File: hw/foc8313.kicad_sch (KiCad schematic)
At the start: 56 parts, among them J1 Tag Connect, J2 CAN, J3 CAN, P1 USB_C_Plug, SW1 SW_SPST, U1 DRV8313PWP, U10 XC6206P332MR, U2 STM32F103CBTx, U4 AS5047D, U6 TJA1044GT/3Z, U7 LMR36015SFBRNXR, X1 X322516MLB4SI

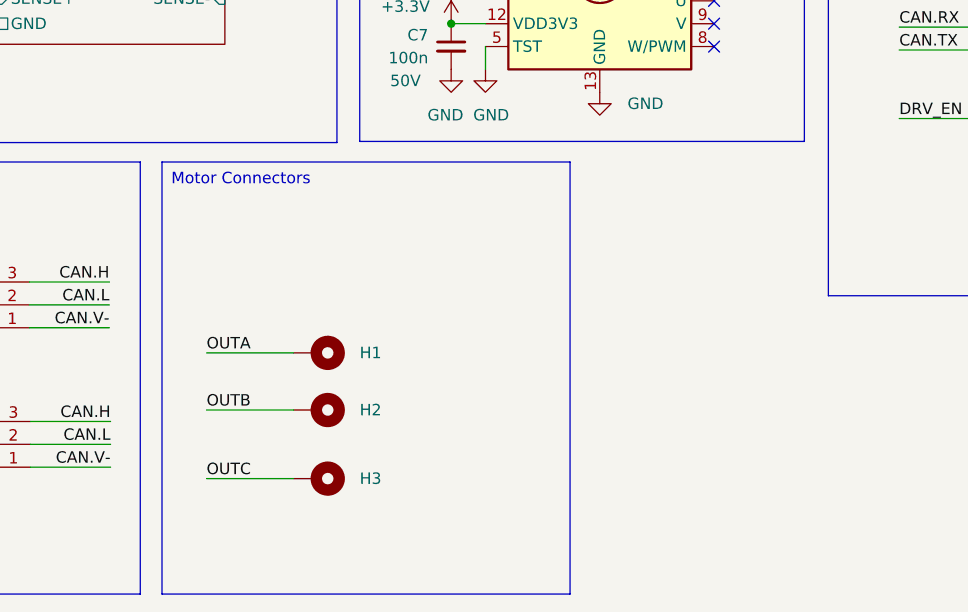
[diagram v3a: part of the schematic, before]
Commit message: [Hw] Rough incomplete layout and component placement
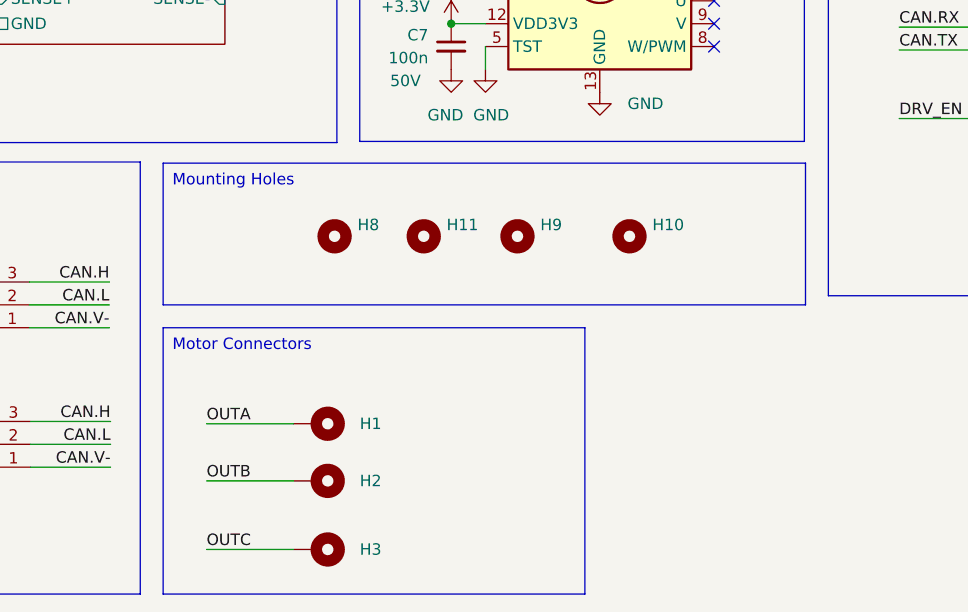
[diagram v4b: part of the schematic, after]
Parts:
- added H10, H11, H8, H9: MountingHole, MountingHole:MountingHole_3.2mm_M3_DIN965_Pad_TopOnly, symbol Mechanical:MountingHole
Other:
- moved on the sheet: H1, H2, H3
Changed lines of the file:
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@@
     (stroke (width 0) (type default))
   )
-  (wire (pts (xy 133.858 182.88) (xy 143.51 182.88))
+  (wire (pts (xy 133.858 190.754) (xy 143.51 190.754))
     (stroke (width 0) (type default))
   )
@@
     (stroke (width 0) (type default))
   )
-  (wire (pts (xy 133.858 175.26) (xy 143.51 175.26))
+  (wire (pts (xy 133.858 183.134) (xy 143.51 183.134))
     (stroke (width 0) (type default))
   )
@@
     (stroke (width 0) (type default))
   )
-  (wire (pts (xy 133.858 168.91) (xy 143.51 168.91))
+  (wire (pts (xy 133.858 176.784) (xy 143.51 176.784))
     (stroke (width 0) (type default))
   )
@@
   )
   (text_box "Motor Connectors\n"
-    (at 128.905 147.701 0) (size 45.339 48.006)
+    (at 129.032 166.116 0) (size 46.863 29.591)
+    (stroke (width 0) (type default))
+    (fill (type none))
+    (effects (font (size 1.27 1.27)) (justify left top))
+  )
+  (text_box "Mounting Holes\n"
+    (at 129.032 147.828 0) (size 71.374 15.748)
     (stroke (width 0) (type default))
     (fill (type none))
@@
     (effects (font (size 1.27 1.27)) (justify right bottom))
   )
-  (label "OUTC" (at 133.858 182.88 0) (fields_autoplaced)
+  (label "OUTC" (at 133.858 190.754 0) (fields_autoplaced)
     (effects (font (size 1.27 1.27)) (justify left bottom))
   )
@@
     (effects (font (size 1.27 1.27)) (justify right bottom))
   )
-  (label "OUTB" (at 133.858 175.26 0) (fields_autoplaced)
+  (label "OUTB" (at 133.858 183.134 0) (fields_autoplaced)
     (effects (font (size 1.27 1.27)) (justify left bottom))
   )
@@
     (effects (font (size 1.27 1.27)) (justify left bottom))
   )
-  (label "OUTA" (at 133.858 168.91 0) (fields_autoplaced)
+  (label "OUTA" (at 133.858 176.784 0) (fields_autoplaced)
     (effects (font (size 1.27 1.27)) (justify left bottom))
   )
@@
     )
   )
-  (symbol (lib_id "Mechanical:MountingHole_Pad") (at 146.05 182.88 270) (unit 1)
+  (symbol (lib_id "Mechanical:MountingHole_Pad") (at 146.05 190.754 270) (unit 1)
     (in_bom yes) (on_board yes) (dnp no) (fields_autoplaced)
-    (property "Reference" "H3" (at 150.876 182.88 90)
+    (property "Reference" "H3" (at 150.876 190.754 90)
       (effects (font (size 1.27 1.27)) (justify left))
     )
-    (property "Value" "MountingHole_Pad" (at 150.876 184.15 90)
+    (property "Value" "MountingHole_Pad" (at 150.876 192.024 90)
       (effects (font (size 1.27 1.27)) (justify left) hide)
     )
-    (property "Footprint" "local_lib:2x3" (at 146.05 182.88 0)
+    (property "Footprint" "local_lib:2x3" (at 146.05 190.754 0)
       (effects (font (size 1.27 1.27)) hide)
     )
-    (property "Datasheet" "~" (at 146.05 182.88 0)
+    (property "Datasheet" "~" (at 146.05 190.754 0)
       (effects (font (size 1.27 1.27)) hide)
     )
@@
     )
   )
+  (symbol (lib_id "Mechanical:MountingHole") (at 157.988 155.956 0) (unit 1)
+    (in_bom yes) (on_board yes) (dnp no) (fields_autoplaced)
+    (property "Reference" "H11" (at 160.528 154.686 0)
+      (effects (font (size 1.27 1.27)) (justify left))
+    )
+    (property "Value" "MountingHole" (at 160.528 157.226 0)
+      (effects (font (size 1.27 1.27)) (justify left) hide)
+    )
+    (property "Footprint" "MountingHole:MountingHole_3.2mm_M3_DIN965_Pad_TopOnly" (at 157.988 155.956 0)
+      (effects (font (size 1.27 1.27)) hide)
+    )
+    (property "Datasheet" "~" (at 157.988 155.956 0)
+      (effects (font (size 1.27 1.27)) hide)
+    )
+    (instances
+      (project "foc8313"
+        (path "/6a0f293a-1ae1-497a-a3c1-0d8f9e6f81b9"
+          (reference "H11") (unit 1)
+        )
+      )
+    )
+  )
   (symbol (lib_id "PCM_Diode_TVS_AKL:SMBJ48CA") (at 24.765 39.37 90) (unit 1)
     (in_bom yes) (on_board yes) (dnp no) (fields_autoplaced)
@@
     )
   )
+  (symbol (lib_id "Mechanical:MountingHole") (at 168.402 155.956 0) (unit 1)
+    (in_bom yes) (on_board yes) (dnp no) (fields_autoplaced)
+    (property "Reference" "H9" (at 170.942 154.686 0)
+      (effects (font (size 1.27 1.27)) (justify left))
+    )
+    (property "Value" "MountingHole" (at 170.942 157.226 0)
+      (effects (font (size 1.27 1.27)) (justify left) hide)
+    )
+    (property "Footprint" "MountingHole:MountingHole_3.2mm_M3_DIN965_Pad_TopOnly" (at 168.402 155.956 0)
+      (effects (font (size 1.27 1.27)) hide)
+    )
+    (property "Datasheet" "~" (at 168.402 155.956 0)
+      (effects (font (size 1.27 1.27)) hide)
+    )
+    (instances
+      (project "foc8313"
+        (path "/6a0f293a-1ae1-497a-a3c1-0d8f9e6f81b9"
+          (reference "H9") (unit 1)
+        )
+      )
+    )
+  )
   (symbol (lib_id "power:GND") (at 268.732 144.018 0) (unit 1)
     (in_bom yes) (on_board yes) (dnp no)
@@
     )
   )
+  (symbol (lib_id "Mechanical:MountingHole") (at 180.848 155.956 0) (unit 1)
+    (in_bom yes) (on_board yes) (dnp no) (fields_autoplaced)
+    (property "Reference" "H10" (at 183.388 154.686 0)
+      (effects (font (size 1.27 1.27)) (justify left))
+    )
+    (property "Value" "MountingHole" (at 183.388 157.226 0)
+      (effects (font (size 1.27 1.27)) (justify left) hide)
+    )
+    (property "Footprint" "MountingHole:MountingHole_3.2mm_M3_DIN965_Pad_TopOnly" (at 180.848 155.956 0)
+      (effects (font (size 1.27 1.27)) hide)
+    )
+    (property "Datasheet" "~" (at 180.848 155.956 0)
+      (effects (font (size 1.27 1.27)) hide)
+    )
+    (instances
+      (project "foc8313"
+        (path "/6a0f293a-1ae1-497a-a3c1-0d8f9e6f81b9"
+          (reference "H10") (unit 1)
+        )
+      )
+    )
+  )
   (symbol (lib_name "+3.3V_3") (lib_id "power:+3.3V") (at 105.41 84.074 0) (unit 1)
     (in_bom yes) (on_board yes) (dnp no)
@@
     )
   )
+  (symbol (lib_id "Mechanical:MountingHole") (at 148.082 155.956 0) (unit 1)
+    (in_bom yes) (on_board yes) (dnp no) (fields_autoplaced)
+    (property "Reference" "H8" (at 150.622 154.686 0)
+      (effects (font (size 1.27 1.27)) (justify left))
+    )
+    (property "Value" "MountingHole" (at 150.622 157.226 0)
+      (effects (font (size 1.27 1.27)) (justify left) hide)
+    )
+    (property "Footprint" "MountingHole:MountingHole_3.2mm_M3_DIN965_Pad_TopOnly" (at 148.082 155.956 0)
+      (effects (font (size 1.27 1.27)) hide)
+    )
+    (property "Datasheet" "~" (at 148.082 155.956 0)
+      (effects (font (size 1.27 1.27)) hide)
+    )
+    (instances
+      (project "foc8313"
+        (path "/6a0f293a-1ae1-497a-a3c1-0d8f9e6f81b9"
+          (reference "H8") (unit 1)
+        )
+      )
+    )
+  )
   (symbol (lib_id "Connector:Conn_ARM_SWD_TagConnect_TC2030-NL") (at 264.795 59.69 270) (mirror x) (unit 1)
     (in_bom no) (on_board yes) (dnp no)
@@
     )
   )
-  (symbol (lib_id "Mechanical:MountingHole_Pad") (at 146.05 175.26 270) (unit 1)
+  (symbol (lib_id "Mechanical:MountingHole_Pad") (at 146.05 183.134 270) (unit 1)
     (in_bom yes) (on_board yes) (dnp no) (fields_autoplaced)
-    (property "Reference" "H2" (at 150.876 175.26 90)
+    (property "Reference" "H2" (at 150.876 183.134 90)
       (effects (font (size 1.27 1.27)) (justify left))
     )
-    (property "Value" "MountingHole_Pad" (at 150.876 176.53 90)
+    (property "Value" "MountingHole_Pad" (at 150.876 184.404 90)
       (effects (font (size 1.27 1.27)) (justify left) hide)
     )
-    (property "Footprint" "local_lib:2x3" (at 146.05 175.26 0)
+    (property "Footprint" "local_lib:2x3" (at 146.05 183.134 0)
       (effects (font (size 1.27 1.27)) hide)
     )
-    (property "Datasheet" "~" (at 146.05 175.26 0)
+    (property "Datasheet" "~" (at 146.05 183.134 0)
       (effects (font (size 1.27 1.27)) hide)
     )
@@
     )
   )
-  (symbol (lib_id "Mechanical:MountingHole_Pad") (at 146.05 168.91 270) (unit 1)
+  (symbol (lib_id "Mechanical:MountingHole_Pad") (at 146.05 176.784 270) (unit 1)
     (in_bom yes) (on_board yes) (dnp no) (fields_autoplaced)
-    (property "Reference" "H1" (at 150.876 168.91 90)
+    (property "Reference" "H1" (at 150.876 176.784 90)
       (effects (font (size 1.27 1.27)) (justify left))
     )
-    (property "Value" "MountingHole_Pad" (at 150.876 170.18 90)
+    (property "Value" "MountingHole_Pad" (at 150.876 178.054 90)
       (effects (font (size 1.27 1.27)) (justify left) hide)
     )
-    (property "Footprint" "local_lib:2x3" (at 146.05 168.91 0)
+    (property "Footprint" "local_lib:2x3" (at 146.05 176.784 0)
       (effects (font (size 1.27 1.27)) hide)
     )
-    (property "Datasheet" "~" (at 146.05 168.91 0)
+    (property "Datasheet" "~" (at 146.05 176.784 0)
       (effects (font (size 1.27 1.27)) hide)
     )

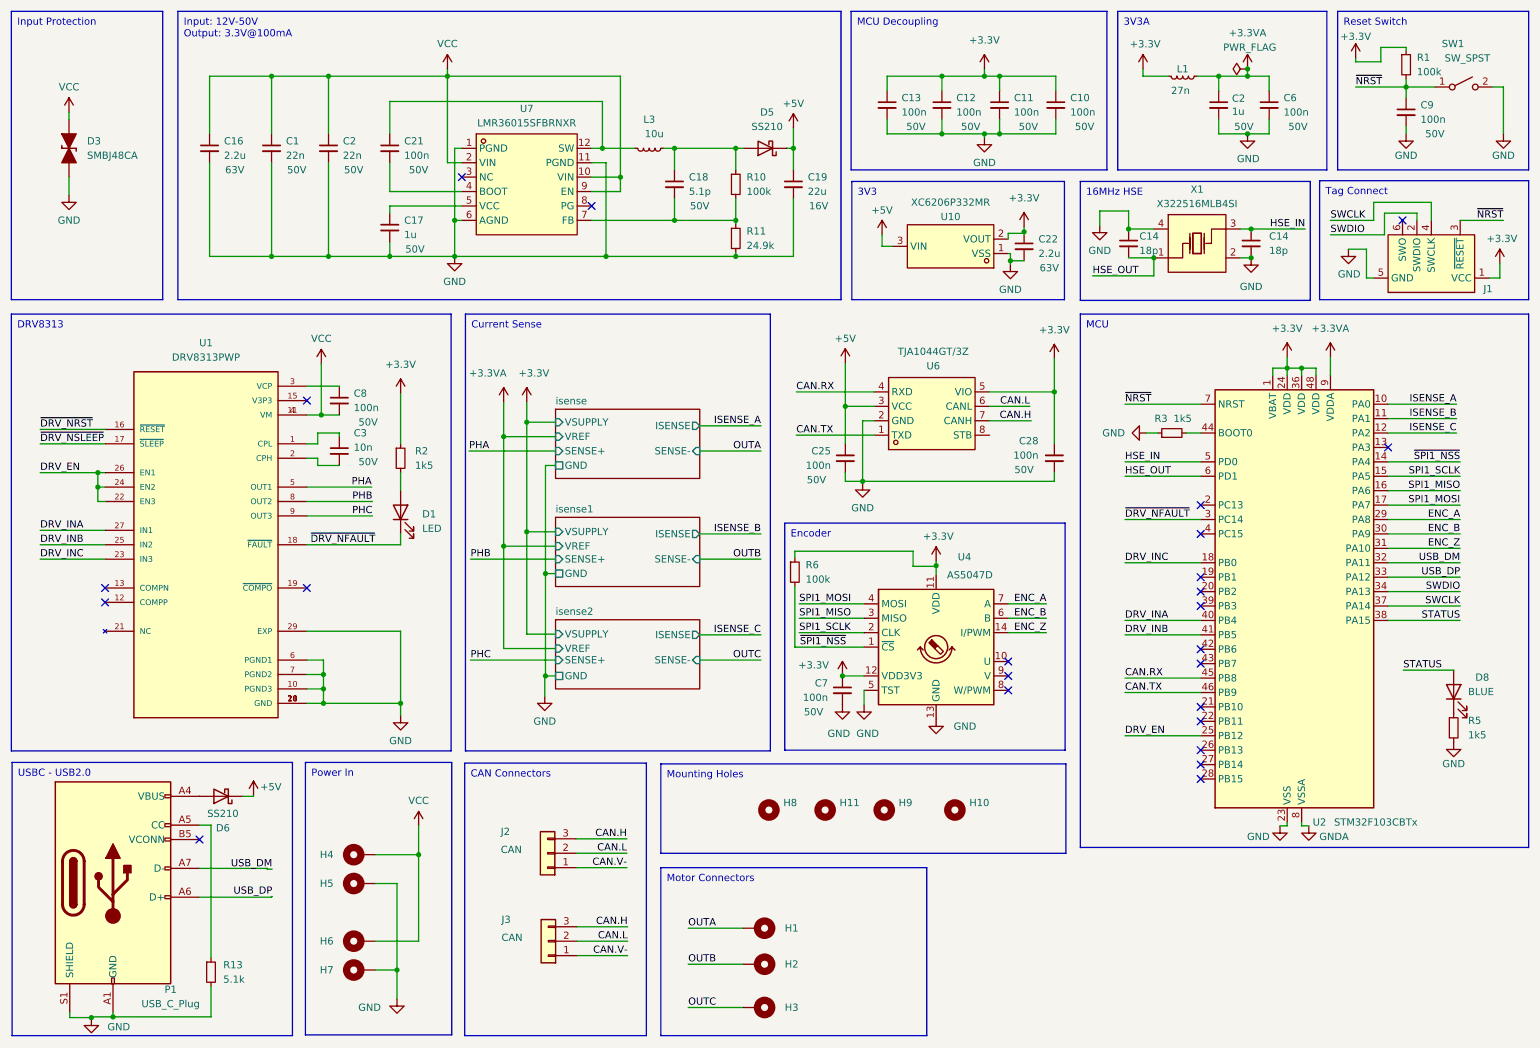
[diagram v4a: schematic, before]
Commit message: [Hw] compact discrete 4 wire iso can, approx drv routing, eeprom
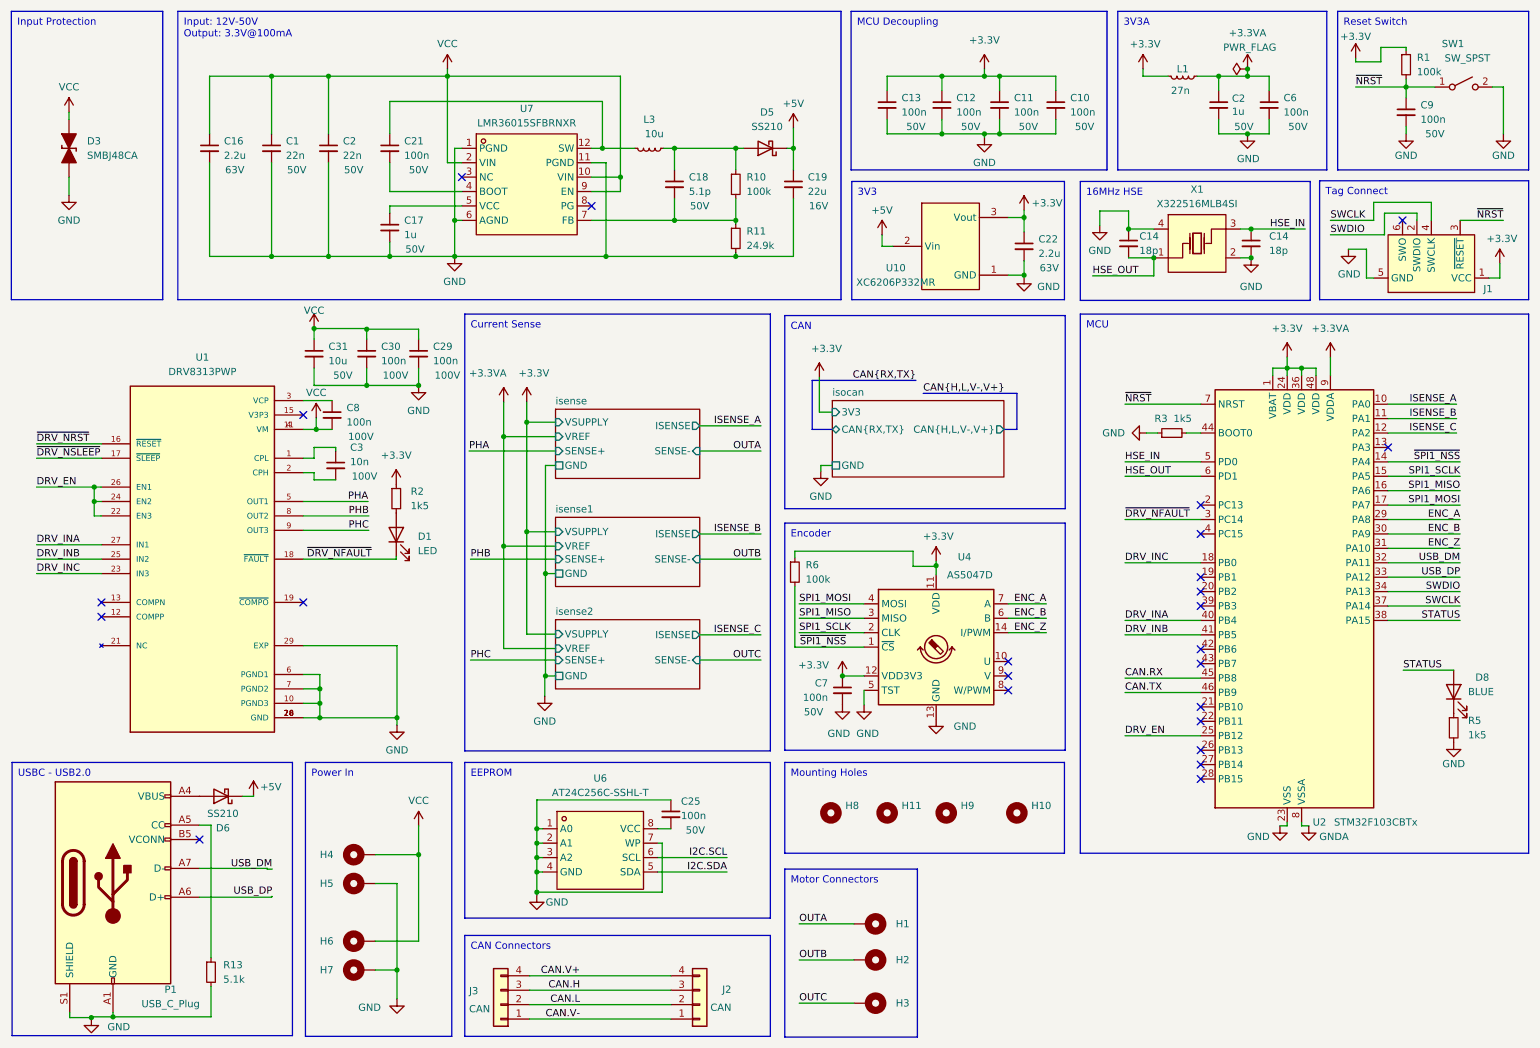
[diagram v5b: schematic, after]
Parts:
- removed C28: 100n, Capacitor_SMD:C_0402_1005Metric, symbol Device:C_Small
- removed J2: CAN, Connector_JST:JST_GH_SM03B-GHS-TB_1x03-1MP_P1.25mm_Horizontal, symbol Connector_Generic:Conn_01x03
- removed U10: XC6206P332MR, easyeda:SOT-23-3_L3.0-W1.7-P0.95-LS2.9-BR, symbol easyeda:XC6206P332MR_C347376
- removed U6: TJA1044GT/3Z, easyeda:SO-8_L4.9-W3.9-P1.27-LS5.9-BL, symbol easyeda:TJA1044GT_3Z
- added C29, C30: 100n, Capacitor_SMD:C_0402_1005Metric, symbol Device:C_Small
- added C31: 10u, Capacitor_SMD:C_1206_3216Metric, symbol Device:C_Small
- added J2: CAN, Connector_JST:JST_GH_SM04B-GHS-TB_1x04-1MP_P1.25mm_Horizontal, symbol Connector_Generic:Conn_01x04
- added U10: XC6206P332MR, easyeda:SOT-23-3_L2.9-W1.6-P1.90-LS2.8-BR, symbol easyeda:XC6206P332MR
- added U6: AT24C256C-SSHL-T, easyeda:SOIC-8_L4.9-W3.9-P1.27-LS6.0-BL, symbol easyeda:AT24C256C-SSHL-T
- C3: LCSC C1546 -> C527014; Rating 50V -> 100V
- C8: LCSC C307331 -> C162178; Rating 50V -> 100V
- J3: footprint Connector_JST:JST_GH_SM03B-GHS-TB_1x03-1MP_P1.25mm_Horizontal -> Connector_JST:JST_GH_SM04B-GHS-TB_1x04-1MP_P1.25mm_Horizontal; symbol Connector_Generic:Conn_01x03 -> Connector_Generic:Conn_01x04; LCSC Part C514175 -> C189895
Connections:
- net +3.3V: now also U10.3 (Vout)
- net +5V: now also U10.2 (Vin); no longer C25.1
- net CAN.H: now also J2.3 (Pin_3)
- net CAN.L: now also J2.2 (Pin_2)
- net CAN.V-: now also J2.1 (Pin_1)
- net GND: now also C25.1, C29.2, C30.2, C31.2, U10.1 (GND), U6.1 (A0), U6.2 (A1), U6.3 (A2), U6.4 (GND), U6.7 (WP); no longer C25.2
- net VCC: now also C29.1, C30.1, C31.1
- new net: C25.2, U6.8 (VCC)
- new net CAN.V+: J2.4 (Pin_4), J3.4 (Pin_4)
- new net I2C.SCL: U6.6 (SCL)
- new net I2C.SDA: U6.5 (SDA)
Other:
- added sheet isocan (isocan.kicad_sch)
- moved on the sheet: C3, C8, D1, H1, H10, H11, H2, H3, H8, H9, R2, U1
